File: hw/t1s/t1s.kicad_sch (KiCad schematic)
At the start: 91 parts, among them J1 SFP edge (INF-8074i), J2 S2B-PH-K-S, U1 GW5AT-LV15MG132C1/I0, U2 GD25Q64CWIGR, U3 TPS62822DLC, U4 TPS22918DBVR, U5 LAN8670C2-E/LMX, U6 TLV75518PDBVR, U7 TLV75512PDBVR, U8 STM32G031F6P6, X1 OB2EL89CLIB112YLC-125M, Y1 25MHz CL12pF 2016

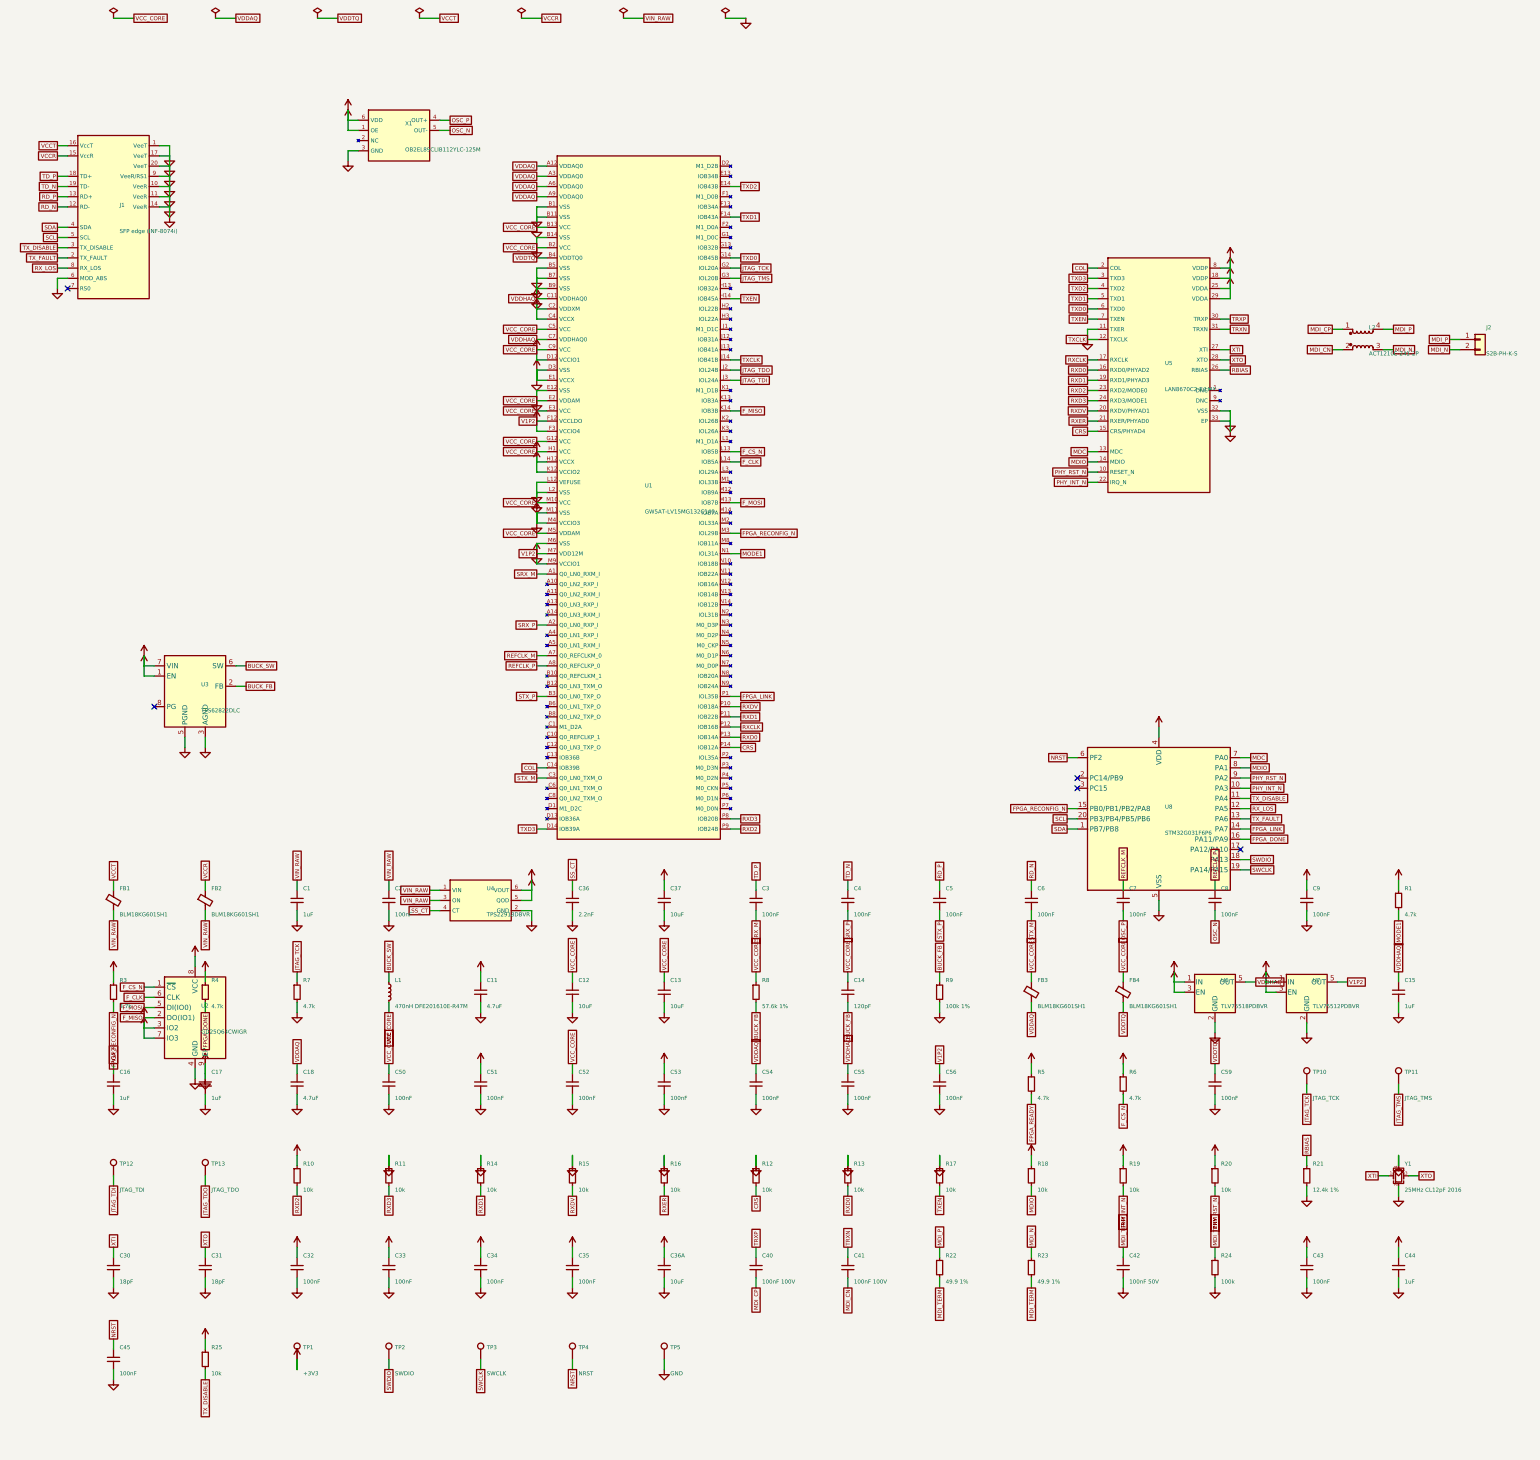
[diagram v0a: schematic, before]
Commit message: T1S: 6-layer board routed and clean, JLC panel and order sheet
- DRC 0 / 0 unconnected (KiCad 7 and 9), schematic parity clean, ERC 0
  errors; gerbers, BOM/CPL, 1:1 print; 5-board panel, DRC clean with the
  board's rules
- the core rail is an In4 island (on In2 it walled the ball field in); In2
  carries two hand-laid buses to the MCU, found once by a maze search and
  baked into make_t1s.py (IN2_BUS)
- JTAG pads beside the FPGA, flash turned 180 degrees, strap/XTO/+3V3 vias in
  the PHY's pads, the MDI pair swapped at the PHY (DME is polarity-free),
  L3/M12 reconnected (they had slipped into a comment)
- MCU pins follow the buses: TX_DISABLE / TX_FAULT on PC14 / PC15 (fw)
- sfpgen: side-pin power stubs no longer turn (GND on TXCLK merged half
  the FPGA's nets in the schematic); ISLANDS as outlines; router vias that
  double a plane dogbone are dropped; T1/RJ45 schematics regenerated,
  both still pass ERC and KiCad 9
- CI: t1s joins the KiCad 9 matrix
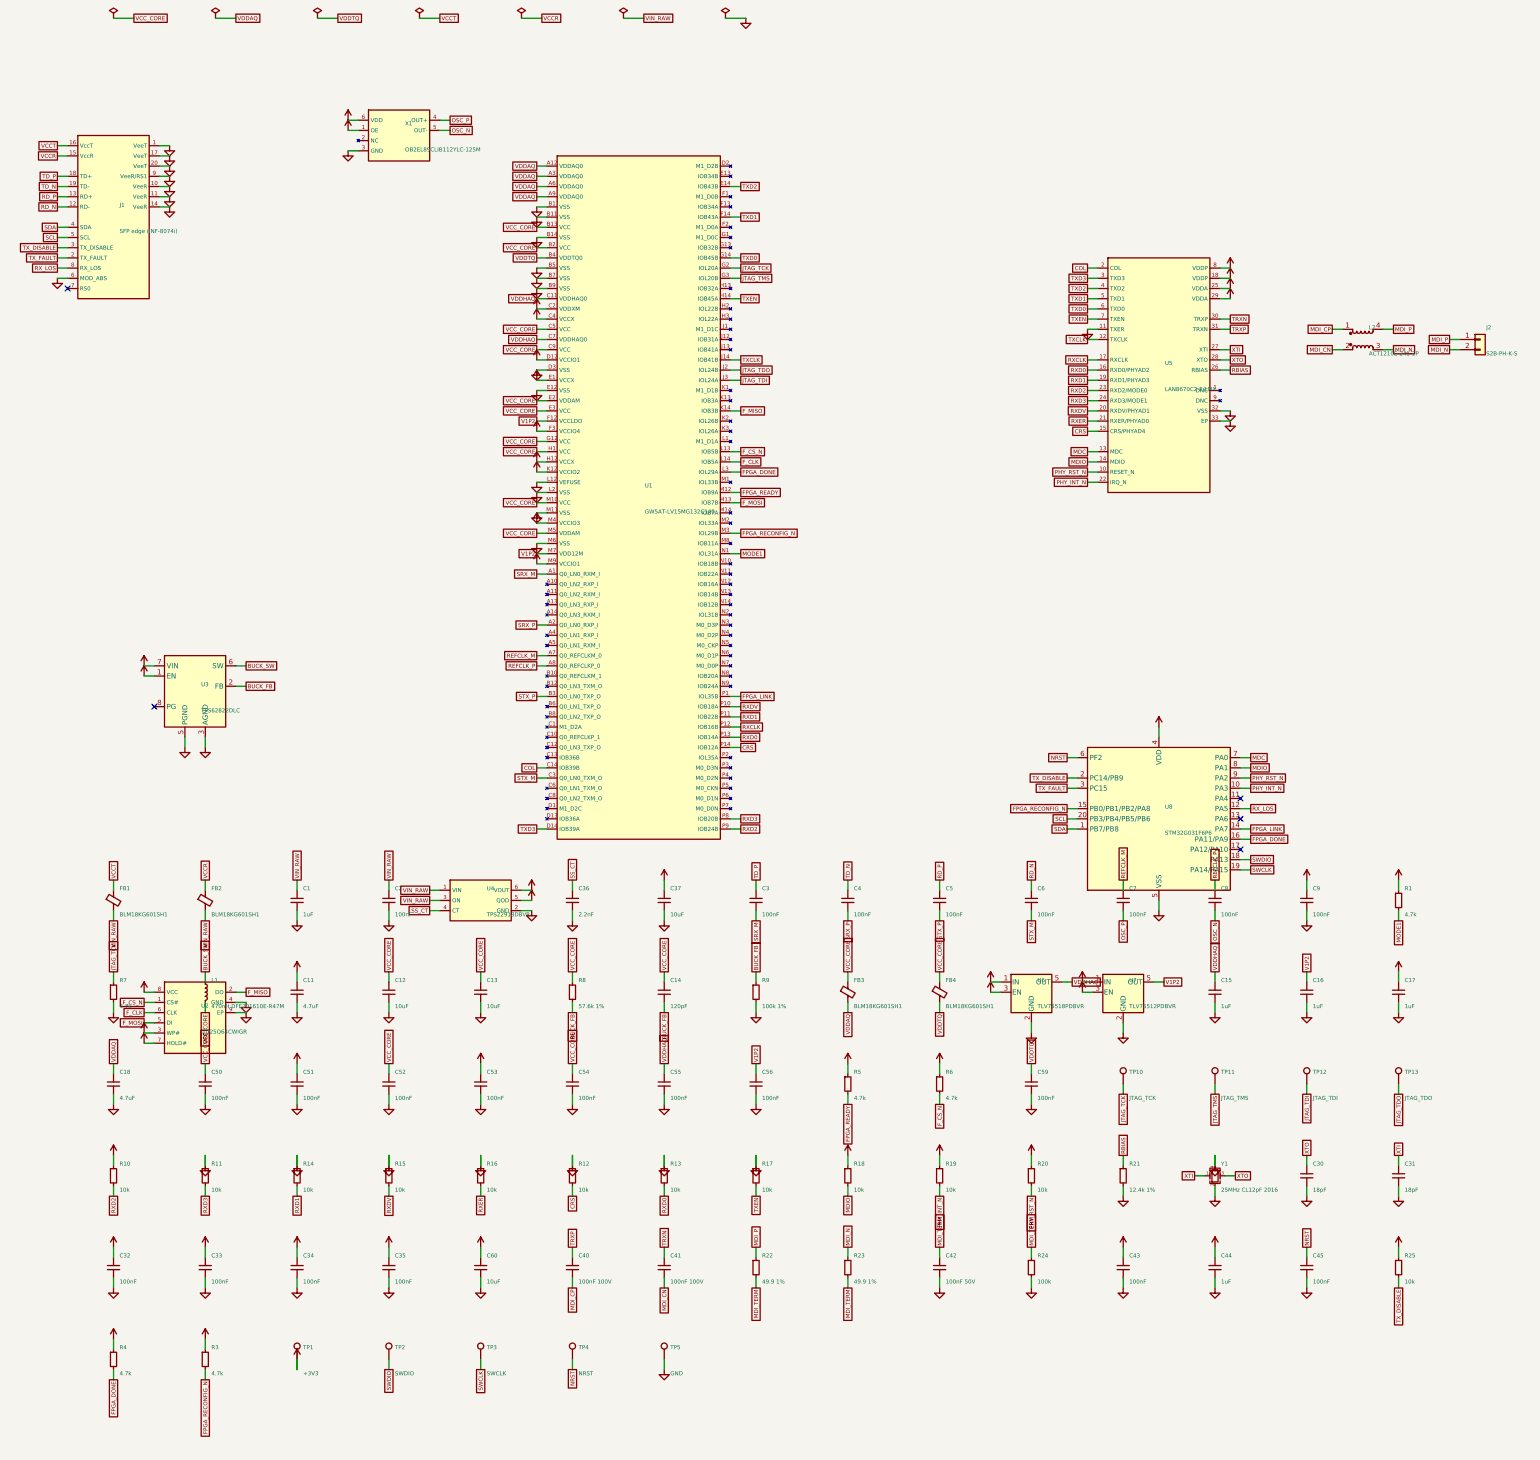
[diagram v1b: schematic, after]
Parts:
- removed C36A: 10uF, Capacitor_SMD:C_0603_1608Metric, symbol Device:C_Small
- added C60: 10uF, Capacitor_SMD:C_0603_1608Metric, symbol Device:C_Small
- R25: footprint Resistor_SMD:R_0402_1005Metric -> Resistor_SMD:R_0201_0603Metric; LCSC C25744 -> C106225
- TP10, TP11, TP12, TP13: footprint TestPoint:TestPoint_Pad_D1.0mm -> sfp:TestPoint_Pad_D1.0mm_NoSilk
- U2: symbol Memory_Flash:W25Q32JVZP -> sfp:GD25Q64_WSON8
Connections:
- net +3V3: now also C60.1; no longer C1.2, C11.2, C12.1, C12.2, C13.1, C13.2, C14.1, C15.1, C15.2, C16.1, C16.2, C17.2, C18.2, C2.2, C30.2, C31.2, C32.2, C33.2, C34.2, C35.2, C36.2, C37.2, C42.2, C43.2, C44.2, C45.2, C50.1, C50.2, C51.2, C52.1, C52.2, C53.2, C54.2, C55.1, C55.2, C56.1, C56.2, C59.2, C9.2, FB3.1, FB4.1, J1.1 (VeeT), J1.10 (VeeR), J1.11 (VeeR), J1.14 (VeeR), J1.17 (VeeT), J1.20 (VeeT), J1.6 (MOD_ABS), J1.9 (VeeR/RS1), L1.2, R11.1, R12.1, R13.1, R14.1, R15.1, R16.1, R17.1, R21.2, R24.2, R7.2, R8.1, R9.2, TP5.1, U1.B1 (VSS), U1.B11 (VSS), U1.B13 (VCC), U1.B14 (VSS), U1.B2 (VCC), U1.B5 (VSS), U1.B7 (VSS), U1.B9 (VSS), U1.C11 (VDDHAQ0), U1.C5 (VCC), U1.C7 (VDDHAQ0), U1.C9 (VCC), U1.D3 (VSS), U1.E12 (VSS), U1.E2 (VDDAM), U1.E3 (VCC), U1.F12 (VCCLDO), U1.G12 (VCC), U1.H1 (VCC), U1.J14 (IOB41B), U1.K14 (IOB3B), U1.L12 (VEFUSE), U1.L2 (VSS), U1.M10 (VCC), U1.M11 (VSS), U1.M5 (VDDAM), U1.M6 (VSS), U1.M7 (VDD12M), U2.2 (DO(IO1)), U2.4 (GND), U2.9 (EP), U3.3 (AGND), U3.5 (PGND), U4.2 (GND), U5.11 (TXER), U5.12 (TXCLK), U5.32 (VSS), U5.33 (EP), U6.2 (GND), U6.5 (OUT), U7.2 (GND), U7.5 (OUT), U8.5 (VSS), X1.3 (GND), Y1.2, Y1.4
- net FPGA_DONE: now also U1.L3 (IOL29A)
- net FPGA_READY: now also U1.M12 (IOB9A)
- net TRXN: now also U5.30 (TRXP); no longer U5.31 (TRXN)
- net TRXP: now also U5.31 (TRXN); no longer U5.30 (TRXP)
- net TX_DISABLE: now also U8.2 (PC14/PB9); no longer U8.11 (PA4)
- net TX_FAULT: now also U8.3 (PC15); no longer U8.13 (PA6)
- net VDDAQ: no longer C54.1
- net XTI: now also C31.1; no longer C30.1
- net XTO: now also C30.1; no longer C31.1
- new net F_MISO: U1.K14 (IOB3B), U2.2 (DO)
- new net GND: C1.2, C11.2, C12.2, C13.2, C15.2, C16.2, C17.2, C18.2, C2.2, C30.2, C31.2, C32.2, C33.2, C34.2, C35.2, C36.2, C37.2, C42.2, C43.2, C44.2, C45.2, C50.2, C51.2, C52.2, C53.2, C54.2, C55.2, C56.2, C59.2, C60.2, C9.2, J1.1 (VeeT), J1.10 (VeeR), J1.11 (VeeR), J1.14 (VeeR), J1.17 (VeeT), J1.20 (VeeT), J1.6 (MOD_ABS), J1.9 (VeeR/RS1), R11.1, R12.1, R13.1, R14.1, R15.1, R16.1, R17.1, R21.2, R24.2, R7.2, R9.2, TP5.1, U1.B1 (VSS), U1.B11 (VSS), U1.B14 (VSS), U1.B5 (VSS), U1.B7 (VSS), U1.B9 (VSS), U1.D3 (VSS), U1.E12 (VSS), U1.L12 (VEFUSE), U1.L2 (VSS), U1.M11 (VSS), U1.M6 (VSS), U2.4 (GND), U2.9 (EP), U3.3 (AGND), U3.5 (PGND), U4.2 (GND), U5.11 (TXER), U5.32 (VSS), U5.33 (EP), U6.2 (GND), U7.2 (GND), U8.5 (VSS), X1.3 (GND), Y1.2, Y1.4
- new net TXCLK: U1.J14 (IOB41B), U5.12 (TXCLK)
- new net V1P2: C16.1, C56.1, U1.F12 (VCCLDO), U1.M7 (VDD12M), U7.5 (OUT)
- new net VCC_CORE: C12.1, C13.1, C14.1, C50.1, C52.1, C54.1, FB3.1, FB4.1, L1.2, R8.1, U1.B13 (VCC), U1.B2 (VCC), U1.C5 (VCC), U1.C9 (VCC), U1.E2 (VDDAM), U1.E3 (VCC), U1.G12 (VCC), U1.H1 (VCC), U1.M10 (VCC), U1.M5 (VDDAM)
- new net VDDHAQ: C15.1, C55.1, U1.C11 (VDDHAQ0), U1.C7 (VDDHAQ0), U6.5 (OUT)
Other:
- moved on the sheet: C11, C12, C13, C14, C15, C16, C17, C18, C30, C31, C32, C33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

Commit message: References checked against the design; the fixes they turned up
docs/REFERENCES.md: the standards, Linux drivers, TI / Realtek / Microchip /
Gowin datasheets, app notes and EVMs, and commercial modules, each with a
table of the design against it.

Fixed from it:
- T1S: CLKHOLD_N (K3) tied high - pulled down during configuration, it would
  have held the flash clock and the FPGA would never load; P1 (also
  SSPI_CS_N) pulled up (R26); AN1718 BIN: 0.75 W end-node resistors (were
  0.25 W), 100 V centre cap (was 50 V), no copper under the CMC
- RJ45 / T1S: buck inductor 1.0 uH (TPS6282x Table 3): the RTL8221B wants
  its core switcher out of pulse skipping, which now starts at ~0.15 A, not
  ~0.33 A
- T1: no copper under the CMC on F/In1 (DP83TG720 8.5); the TC812 loadout
  fits the 200 uH CMC its datasheet asks for
- fw: PHY settings 70 ms after reset release (TG720: 65 ms before the first
  MDIO frame) with the 0x56 bridge answering 0xFFFF until then; LAN8670 set-up
  picked by silicon revision (AN1699 Rev G: C2 or D0); collision detection
  follows PLCA as AN1699 asks

All three boards: DRC 0 / 0 unconnected, KiCad 9 PASS, panels clean.
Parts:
- added R26: 4.7k, Resistor_SMD:R_0201_0603Metric, symbol Device:R_Small
- C42: value 100nF 50V -> 100nF 100V; LCSC C49678 -> C28233
- L1: value 470nH DFE201610E-R47M -> 1uH DFE201610E-1R0M; LCSC C269773 -> C161082; MPN DFE201610E-R47M -> DFE201610E-1R0M
- R22, R23: value 49.9 1% -> 49.9 1% 0.75W; LCSC C18018 -> C4014562; MPN (none) -> CRCW120649R9FKEAHP
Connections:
- net +3V3: now also U1.K3 (IOL26A), R26.1
- net FPGA_LINK: now also R26.2
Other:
- moved on the sheet: TP1, TP2, TP3, TP4, TP5

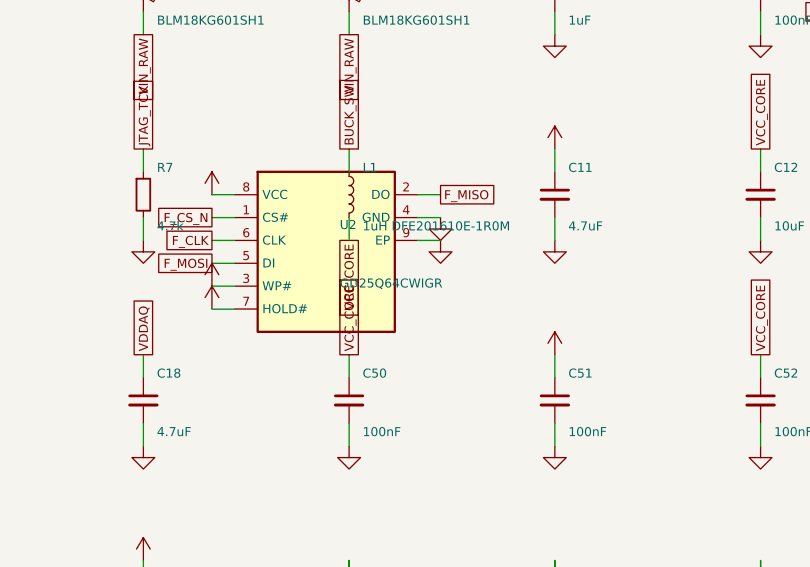
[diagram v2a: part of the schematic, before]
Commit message: Review fixes: 100 V MDI DC block, 128 Mbit flash, T1S MDI geometry
- T1 C33/C34: 100 nF 100 V X5R 0402 (GRM155R62A104KE14D, C162178), split
  from the 16 V decap line (C1525) they had been grouped with
- T1 R6/R7: 1 k 1 % 0.2 W anti-surge 0402 (C313354) instead of 62.5 mW;
  still short of TI's 0.75 W 2010, documented
- T1S U2: GD25Q128EWIGR (C2982923), same WSON-8 footprint, so Gowin's
  default golden address 0x800000 is inside the part; ORDER.md gives the
  flash layout
- compliance.py: each lane's geometry comes from its routed track width;
  the T1S MDI is two 0.2 mm lines (Z0 44.8) with its own delay and loss,
  and an unsolved width now stops the run
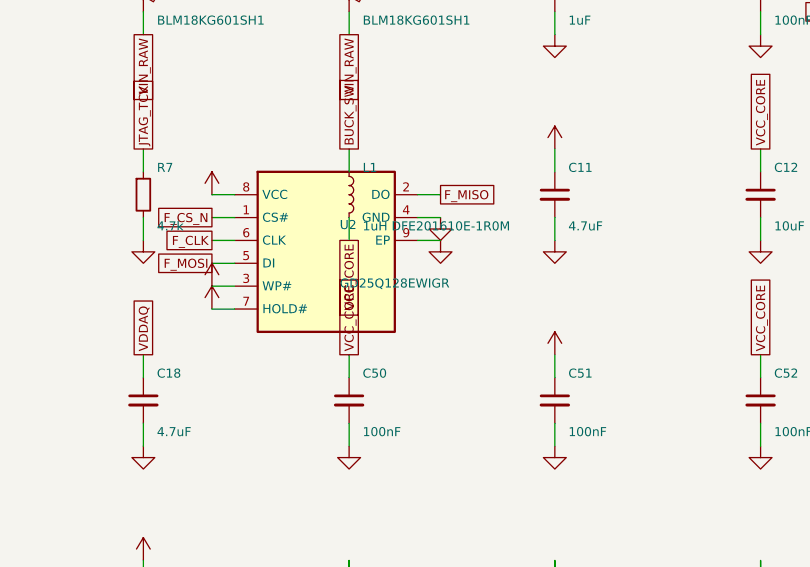
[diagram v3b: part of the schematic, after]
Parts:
- U2: value GD25Q64CWIGR -> GD25Q128EWIGR; symbol sfp:GD25Q64_WSON8 -> sfp:GD25Q128_WSON8; LCSC C395511 -> C2982923; MPN GD25Q64CWIGR -> GD25Q128EWIGR
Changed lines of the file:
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@@
     (instances (project "t1s" (path "/5e1f3a92-7b6c-4d8e-9f01-2a3b4c5d6e71" (reference "#PWR043") (unit 1))))
   )
-  (symbol (lib_id "sfp:GD25Q64_WSON8") (at 59.69 279.40 0) (unit 1)
+  (symbol (lib_id "sfp:GD25Q128_WSON8") (at 59.69 279.40 0) (unit 1)
     (in_bom yes) (on_board yes) (dnp no)
     (property "Reference" "U2" (at 61.19 276.40 0) (effects (font (size 1.0 1.0)) (justify left)))
-    (property "Value" "GD25Q64CWIGR" (at 61.19 282.90 0) (effects (font (size 1.0 1.0)) (justify left)))
+    (property "Value" "GD25Q128EWIGR" (at 61.19 282.90 0) (effects (font (size 1.0 1.0)) (justify left)))
     (property "Footprint" "Package_SON:WSON-8-1EP_6x5mm_P1.27mm_EP3.4x4.3mm" (at 59.69 279.40 0) (effects (font (size 1.0 1.0)) hide))
     (property "Datasheet" "" (at 59.69 279.40 0) (effects (font (size 1.0 1.0)) hide))
-    (property "MPN" "GD25Q64CWIGR" (at 59.69 279.40 0) (effects (font (size 1.0 1.0)) hide))
-    (property "LCSC" "C395511" (at 59.69 279.40 0) (effects (font (size 1.0 1.0)) hide))
+    (property "MPN" "GD25Q128EWIGR" (at 59.69 279.40 0) (effects (font (size 1.0 1.0)) hide))
+    (property "LCSC" "C2982923" (at 59.69 279.40 0) (effects (font (size 1.0 1.0)) hide))
     (pin "8")
     (pin "1")
